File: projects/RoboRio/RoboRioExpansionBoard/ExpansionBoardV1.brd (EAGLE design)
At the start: 100.3 x 80.3 mm, 68 parts, among them IC1 MCP3008, Q1 5MHz

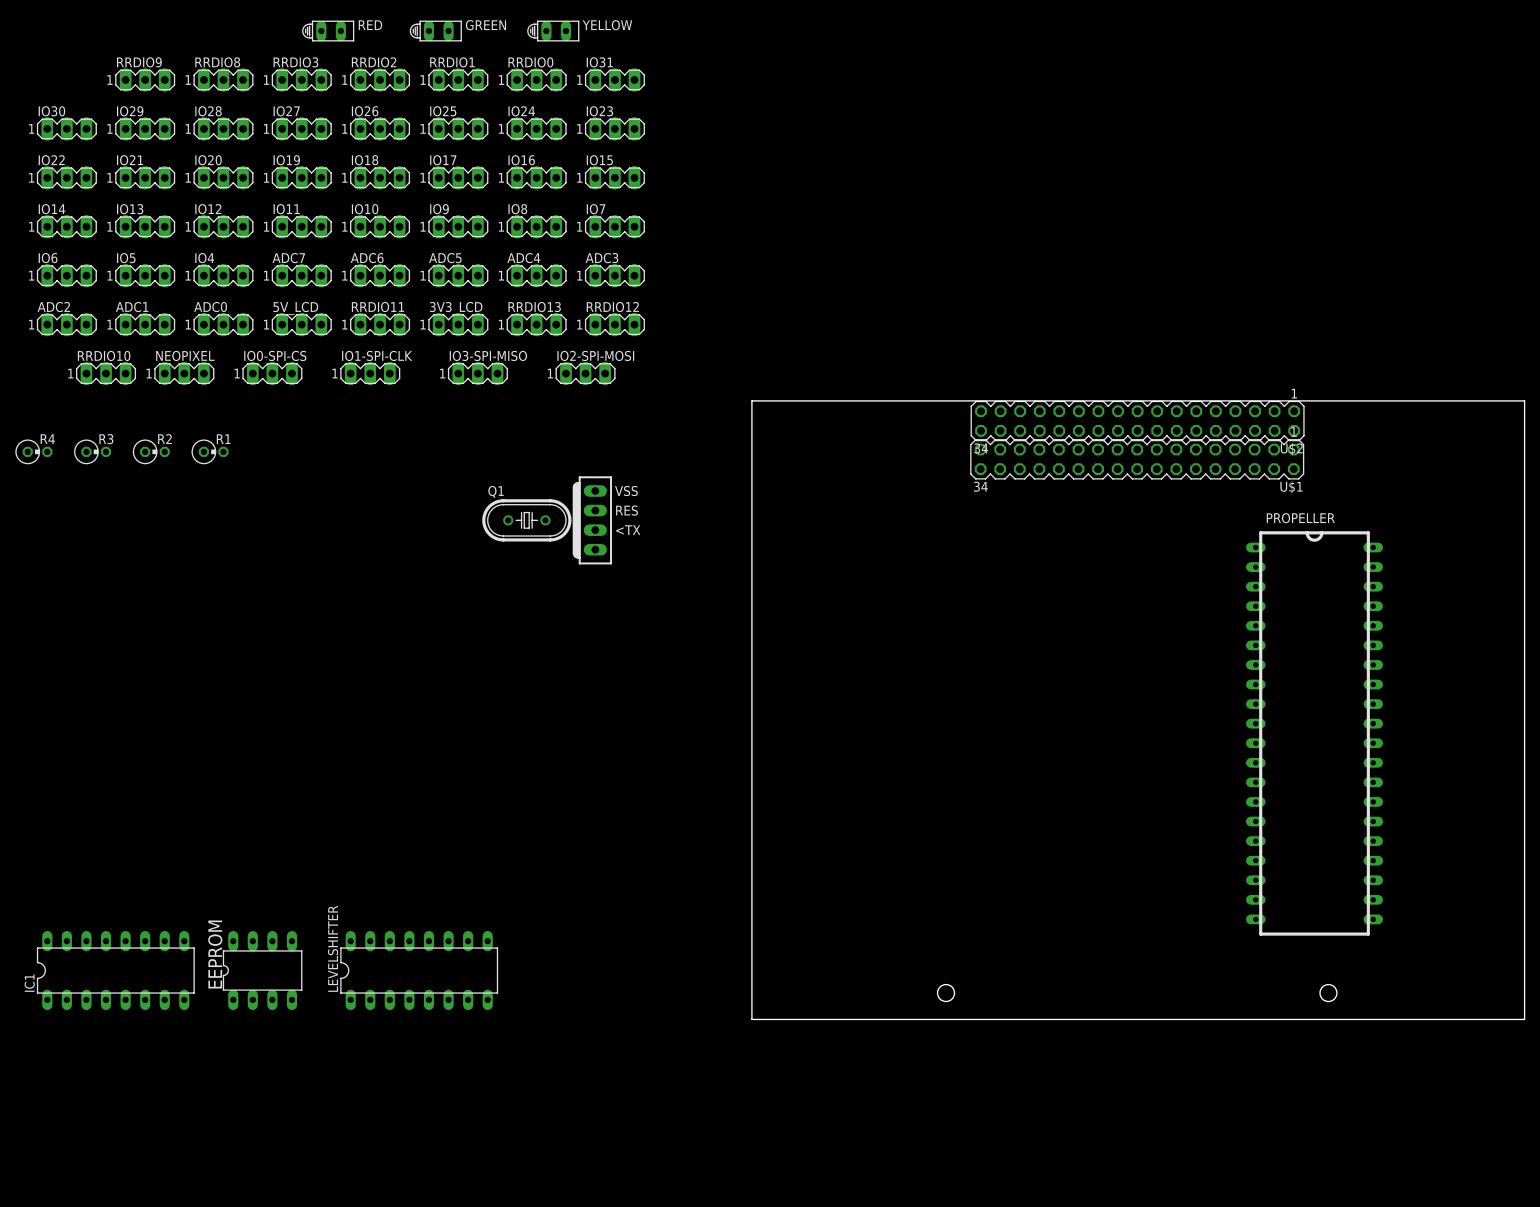
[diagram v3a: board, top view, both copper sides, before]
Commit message: Some IO have been converted to new package
Also added the new package
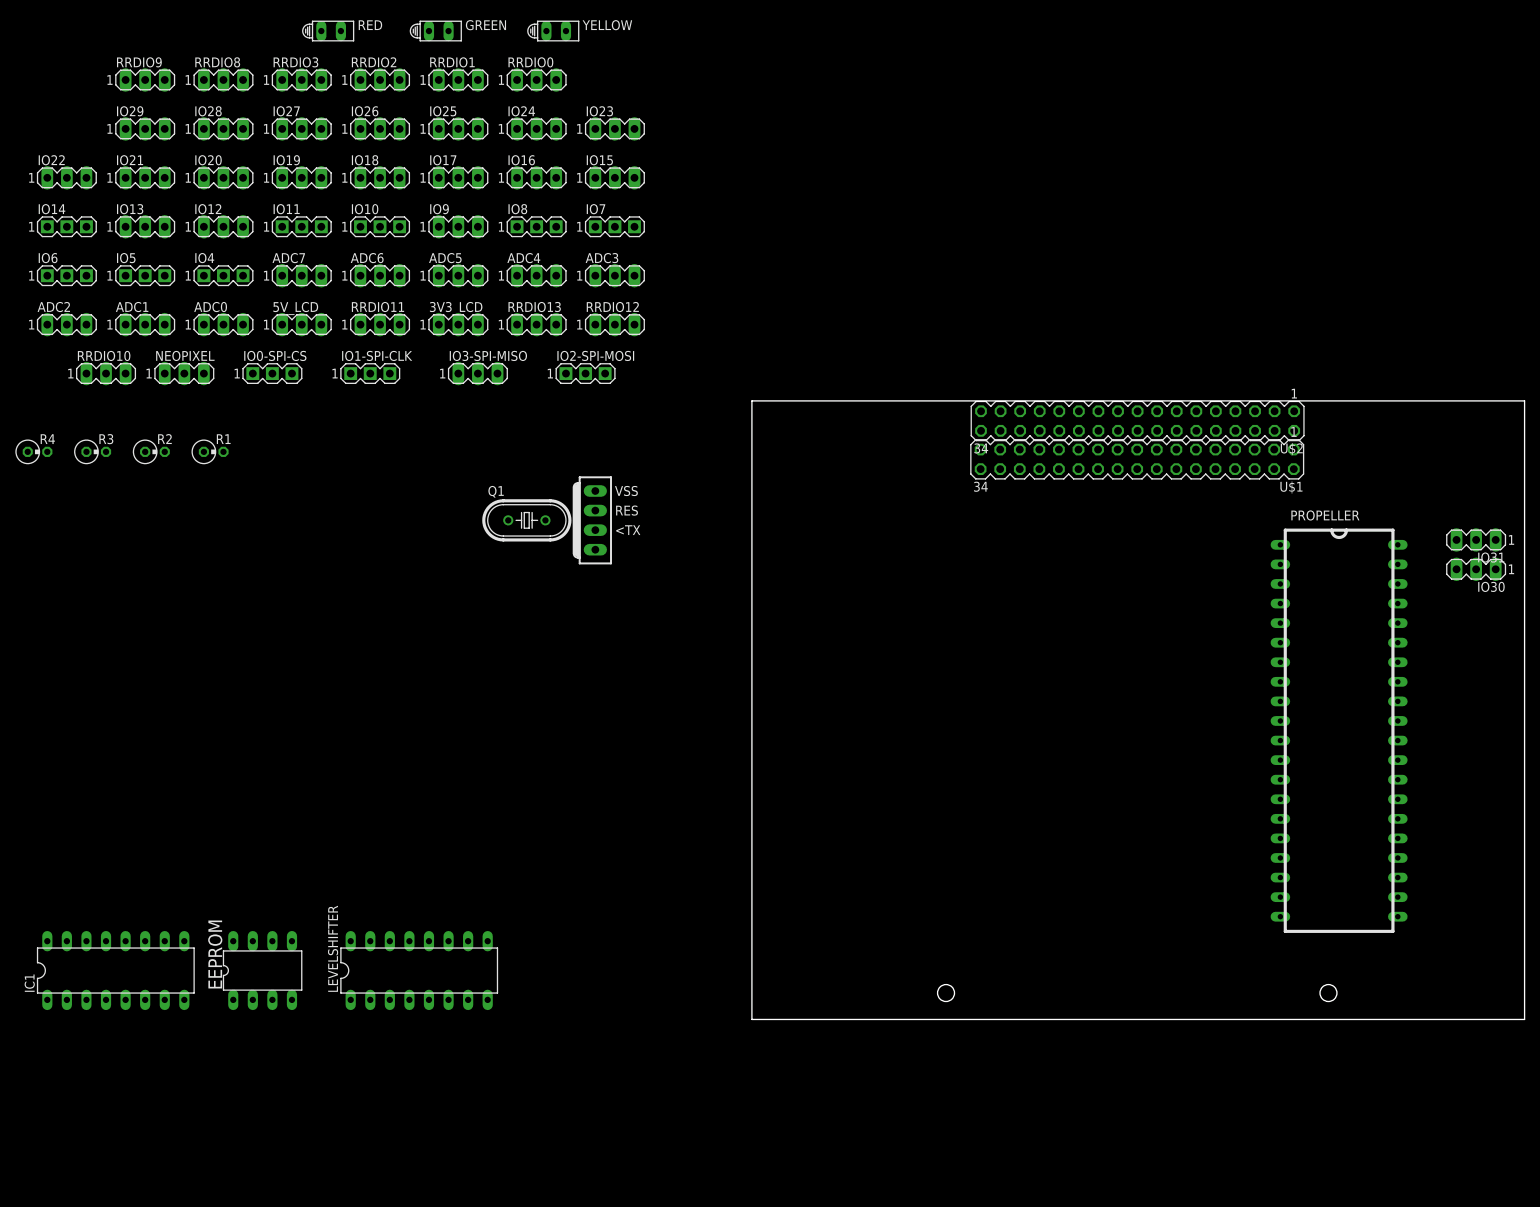
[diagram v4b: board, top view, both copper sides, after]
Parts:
- IO0-SPI-CS, IO1-SPI-CLK, IO10, IO11, IO14, IO2-SPI-MOSI, IO4, IO5, IO6, IO7, IO8: device con-lstb:MA03-1 -> con-lstb-modified:MA03-1
- moved IO30 191.6 mm to (94.0, 58.4), turned to 180 degrees
- moved IO31 126.7 mm to (94.0, 62.2), turned to 180 degrees
- moved PROPELLER 3.21 mm to (76.2, 38.1)

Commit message: Replaced all 3 pin connectors with the new version
using find/replace.  Also attached all ot the ADC input pins
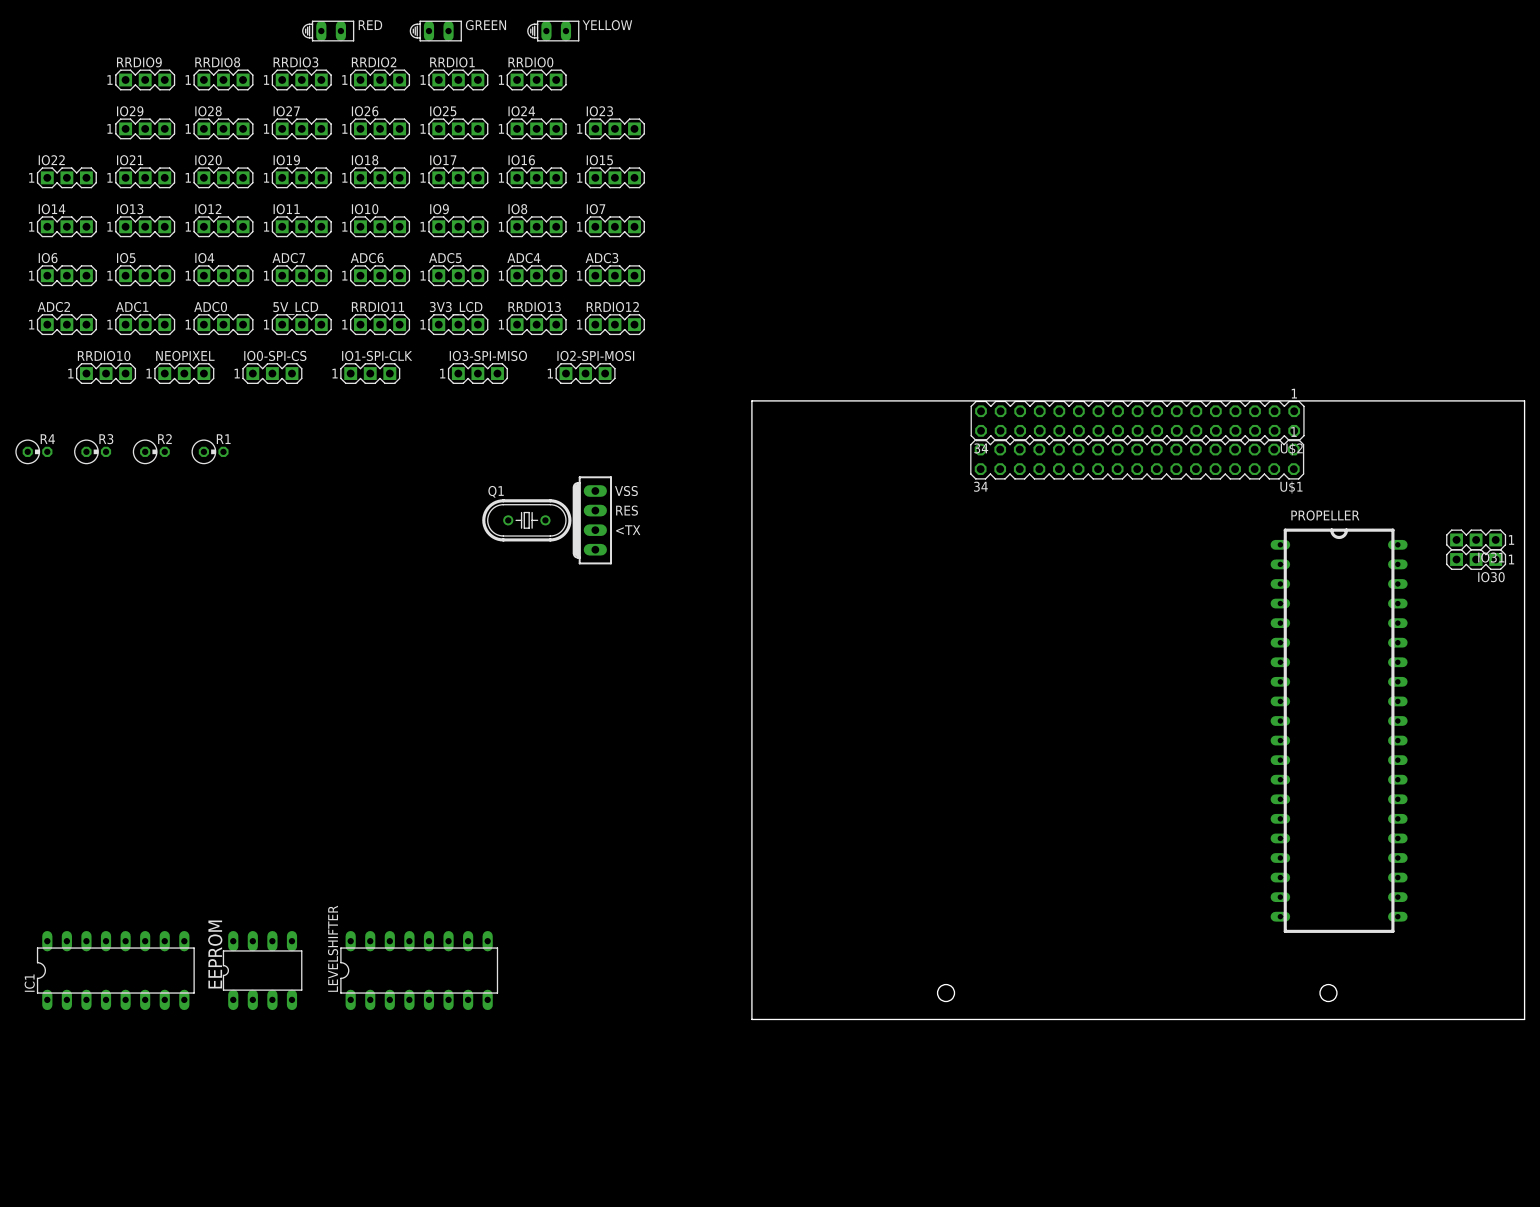
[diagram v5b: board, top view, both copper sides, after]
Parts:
- 3V3_LCD, 5V_LCD, ADC0, ADC1, ADC2, ADC3, ADC4, ADC5, ADC6, ADC7, IO12, IO13, IO15, IO16, IO17, IO18, IO19, IO20, IO21, IO22, IO23, IO24, IO25, IO26, IO27, IO28, IO29, IO3-SPI-MISO, IO30, IO31, IO9, NEOPIXEL, RRDIO0, RRDIO1, RRDIO10, RRDIO11, RRDIO12, RRDIO13, RRDIO2, RRDIO3, RRDIO8, RRDIO9: device con-lstb:MA03-1 -> con-lstb-modified:MA03-1
- moved IO30 1.27 mm to (94.0, 59.7)
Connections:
- new net N$3: ADC7.3, IC1.8
- new net N$4: ADC6.3, IC1.7
- new net N$7: ADC3.3, IC1.4
- new net N$9: ADC1.3, IC1.2
- net N$5: now also ADC5.3
- net N$6: now also ADC4.3

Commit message: found correct package for LEDs
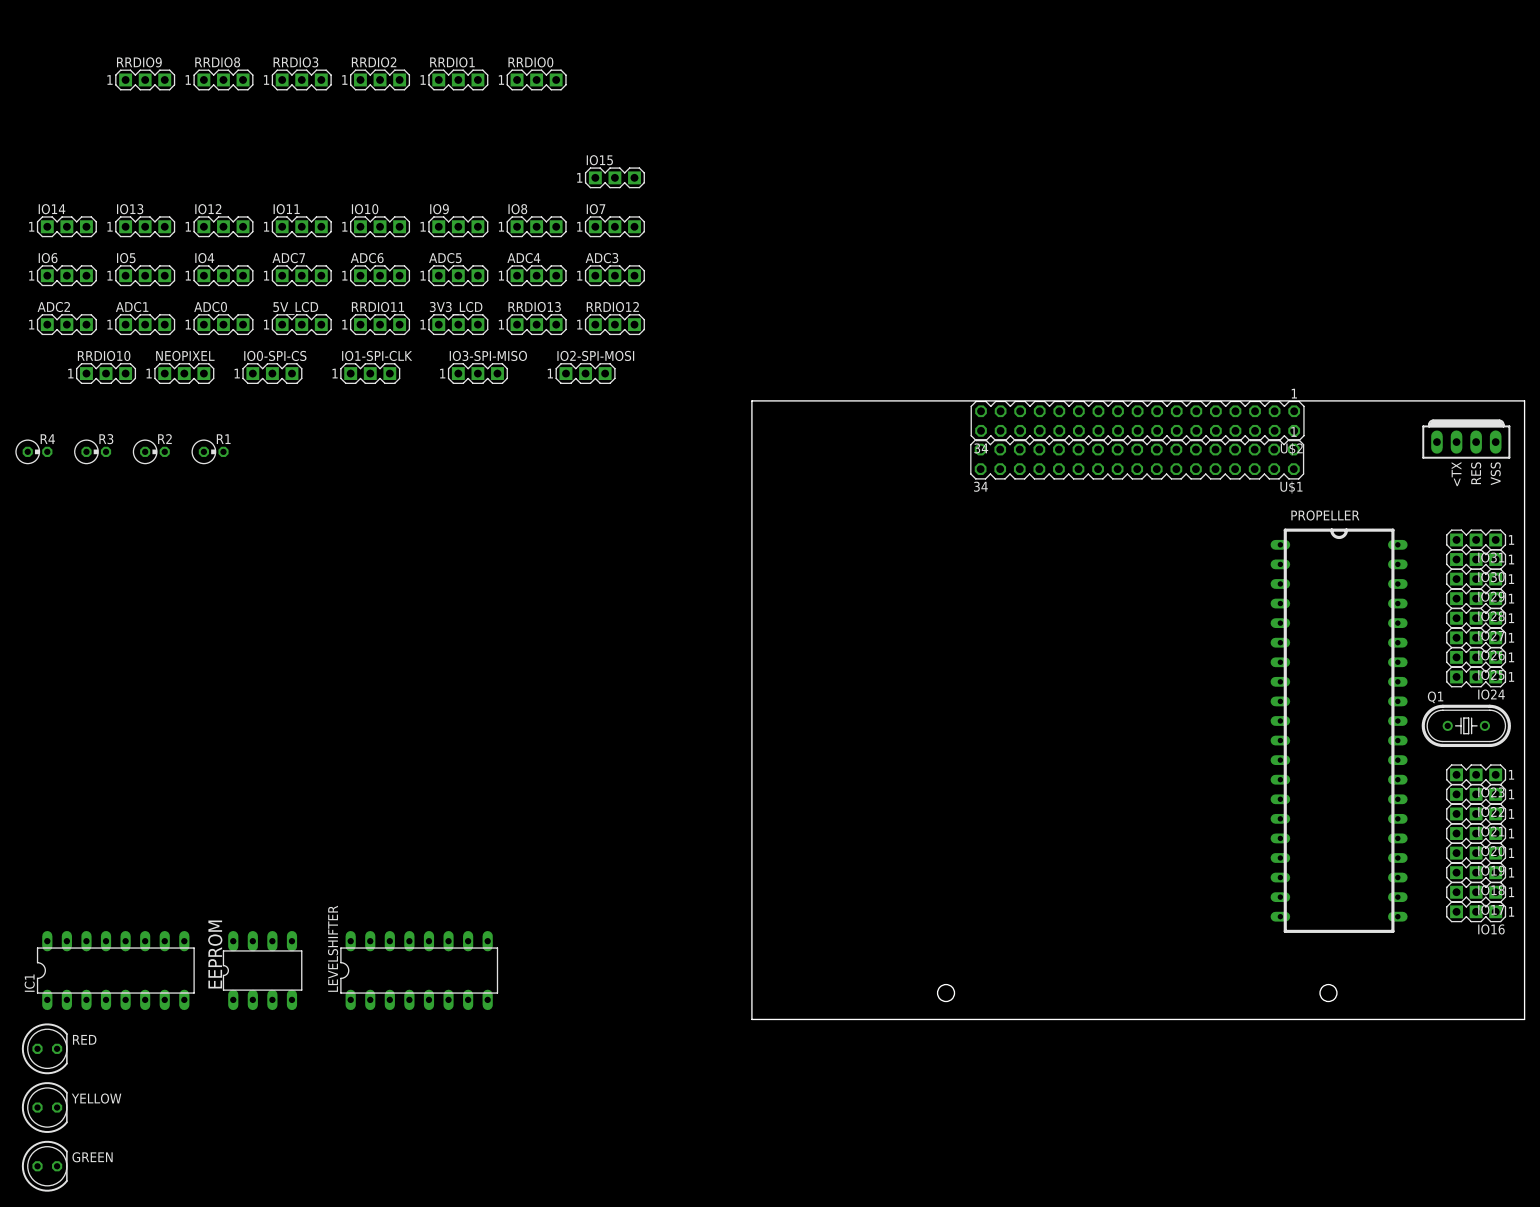
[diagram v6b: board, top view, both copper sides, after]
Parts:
- GREEN, RED, YELLOW: value HLMP6 -> (none); device display-hp:HLMP6 -> led:LED5MM
- moved IO22 199.6 mm to (94.0, 29.2), turned to 180 degrees
- moved IO21 191.4 mm to (94.0, 26.7), turned to 180 degrees
- moved IO20 183.5 mm to (94.0, 24.1), turned to 180 degrees
- moved IO29 182.3 mm to (94.0, 57.1), turned to 180 degrees
- moved IO19 175.8 mm to (94.0, 21.6), turned to 180 degrees
- moved IO28 173.6 mm to (94.0, 54.6), turned to 180 degrees
- moved IO18 168.4 mm to (94.0, 19.1), turned to 180 degrees
- moved IO27 165.1 mm to (94.0, 52.1), turned to 180 degrees
- moved IO17 161.4 mm to (94.0, 16.5), turned to 180 degrees
- moved IO26 156.8 mm to (94.0, 49.5), turned to 180 degrees
- moved GREEN 155.8 mm to (-91.4, -19.1)
- moved IO16 154.7 mm to (94.0, 14.0), turned to 180 degrees
- moved YELLOW 154.5 mm to (-91.4, -11.4)
- moved IO25 148.8 mm to (94.0, 47.0), turned to 180 degrees
- moved IO24 141.1 mm to (94.0, 44.5), turned to 180 degrees
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
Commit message: added EEPROM to board
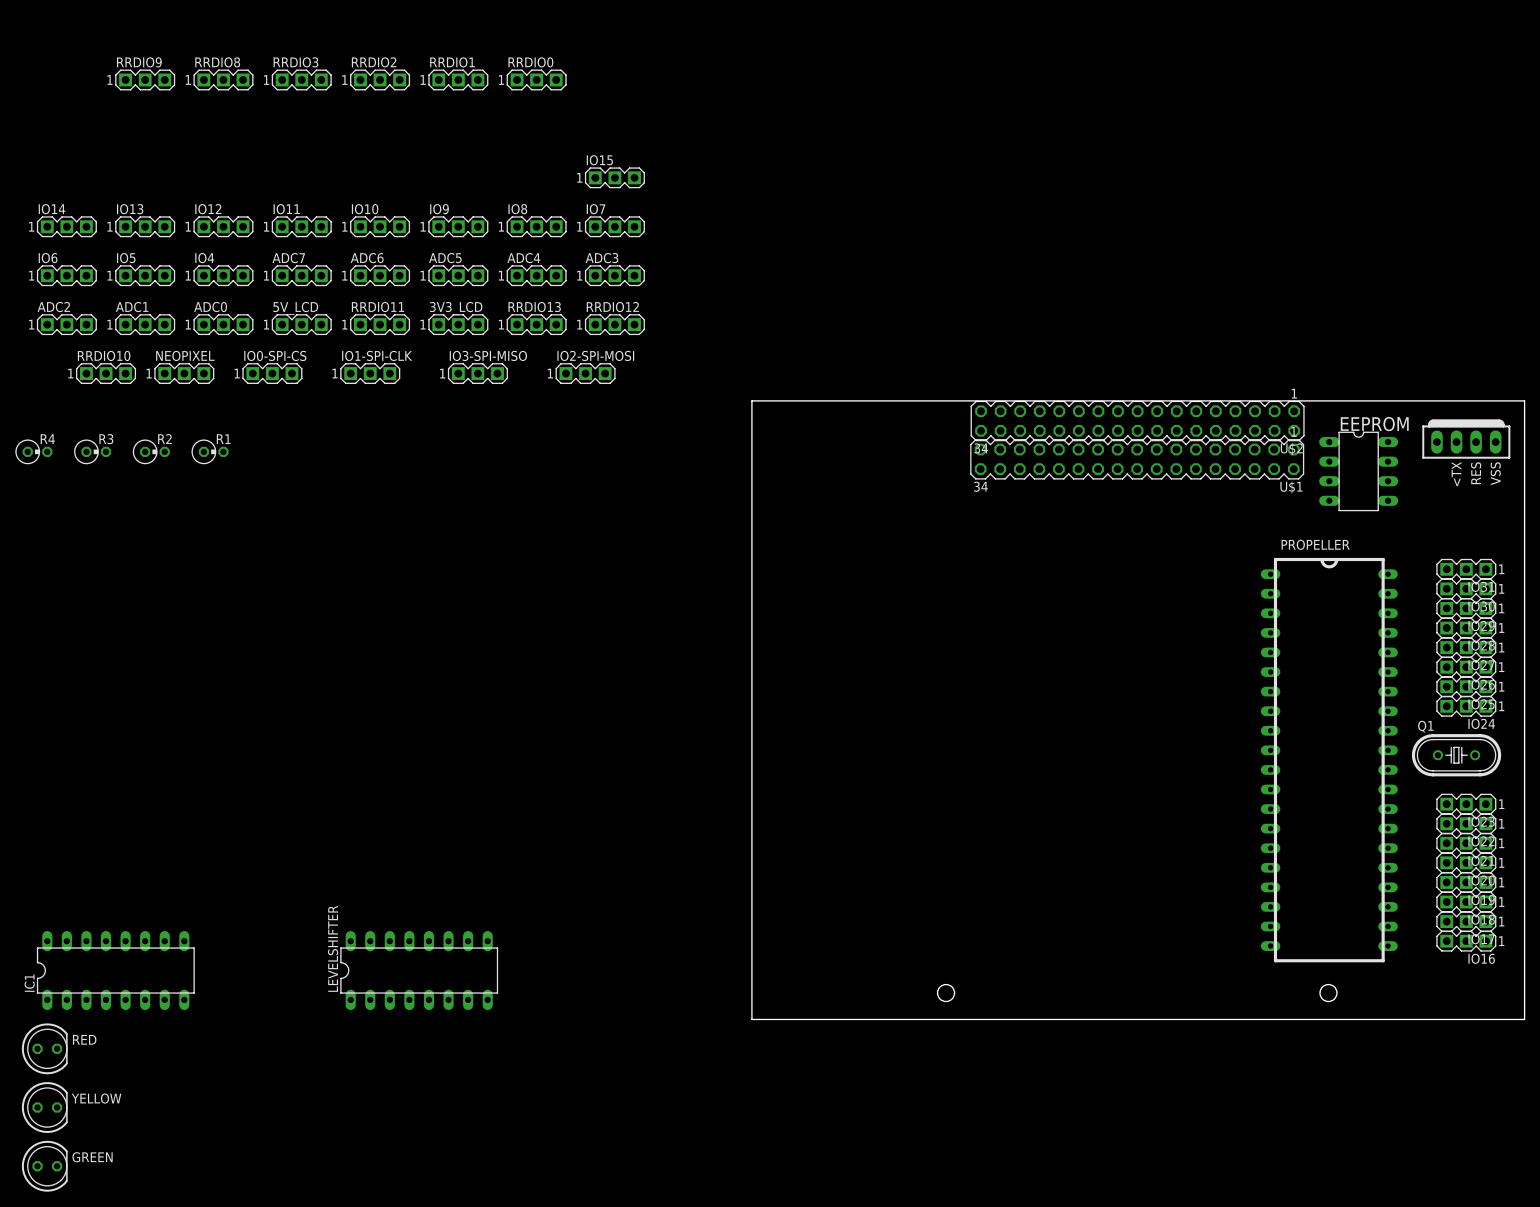
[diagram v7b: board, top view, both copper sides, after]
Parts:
- moved EEPROM 156.3 mm to (78.7, 71.1), turned to 270 degrees
- moved IO17 4.02 mm to (92.7, 12.7)
- moved IO21 4.02 mm to (92.7, 22.9)
- moved IO22 4.02 mm to (92.7, 25.4)
- moved IO24 4.02 mm to (92.7, 40.6)
- moved IO25 4.02 mm to (92.7, 43.2)
- moved IO26 4.02 mm to (92.7, 45.7)
- moved IO27 4.02 mm to (92.7, 48.3)
- moved IO28 4.02 mm to (92.7, 50.8)
- moved IO16 4.02 mm to (92.7, 10.2)
- moved IO18 4.02 mm to (92.7, 15.2)
- moved IO19 4.02 mm to (92.7, 17.8)
- moved IO20 4.02 mm to (92.7, 20.3)
- moved IO23 4.02 mm to (92.7, 27.9)
- moved PROPELLER 4.02 mm to (74.9, 34.3)
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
